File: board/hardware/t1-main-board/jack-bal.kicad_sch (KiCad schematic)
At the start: 6 parts, among them J3901 GT-3321667P-01

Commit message: Board: capture blk.mic-ambient and links #34, #35
IM73D122 on PDM CLK1 and SDI1 (BOM v1 line 34, pinout v1 AK2 and 1P2),
LR to ground, 22 Ω clock series, VDD from MIC_1V8 through link #35.
Link #34 on blk.mic-main makes the faceplate branch the rail MIC_1V8_FP
for contact 40 (power tree §4.12, G10). kicad-lib moves to e46bda4 for
the IM73D122, TPS3808G01, SN74LVC1G58 and BAT54 parts.

Co-Authored-By: Claude Opus 5.5 <noreply@anthropic.com>
Claude-Session: https://claude.ai/code/session_01Ei262h3TpgY9vyfNLMi5Mn
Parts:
- removed D3901, D3902, D3903, D3904, D3905: TPD1E10B06, Package_SON:Texas_DPY0002A_0.6x1mm_P0.65mm, symbol Device:D_TVS
- removed J3901: GT-3321667P-01, G_Switch:G_Switch_GT-3321667P-01_Jack_4.4mm_5Pole_Horizontal, symbol G_Switch:GT-3321667P-01
- added D4001, D4002, D4003, D4004, D4005: TPD1E10B06, Package_SON:Texas_DPY0002A_0.6x1mm_P0.65mm, symbol Device:D_TVS
- added J4001: GT-3321667P-01, G_Switch:G_Switch_GT-3321667P-01_Jack_4.4mm_5Pole_Horizontal, symbol G_Switch:GT-3321667P-01
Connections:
- net GND: now also D4001.1 (A1), D4002.1 (A1), D4003.1 (A1), D4004.1 (A1), D4005.1 (A1), J4001.1 (GND), J4001.9 (SWITCH)
- net HPBAL_L_N: now also D4002.2 (A2), J4001.6 (L-)
- net HPBAL_L_P: now also D4001.2 (A2), J4001.7 (L+), J4001.8 (L+)
- net HPBAL_R_N: now also D4004.2 (A2), J4001.2 (R-), J4001.3 (R-)
- net HPBAL_R_P: now also D4003.2 (A2), J4001.4 (R+), J4001.5 (R+)
- net HP_DET_BAL: now also D4005.2 (A2), J4001.10 (DETECT)
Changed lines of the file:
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@@
 (title_block (title "4.4 mm headphone jack") (date "2026-10-25") (rev "A") (company "The OpenDAP Project") (comment 1 "blk.jack-bal") (comment 2 "Balanced output jack (JEITA RC-8141C) with ESD and plug detect"))
 (symbol (lib_id "G_Switch:GT-3321667P-01") (at 52.07 64.77 0) (unit 1) (body_style 1) (exclude_from_sim no) (in_bom yes) (on_board yes) (dnp no)
-  (property "Reference" "J3901" (at 43.18 43.18 0) (effects (font (size 1.27 1.27)) (justify left)))
+  (property "Reference" "J4001" (at 43.18 43.18 0) (effects (font (size 1.27 1.27)) (justify left)))
   (property "Value" "GT-3321667P-01" (at 43.18 40.64 0) (effects (font (size 1.27 1.27)) (justify left)))
   (property "Footprint" "G_Switch:G_Switch_GT-3321667P-01_Jack_4.4mm_5Pole_Horizontal" (at 52.07 64.77 0) (effects (font (size 1.27 1.27))) (hide yes))
@@
   (pin "9")
   (pin "1")
-  (instances (project "t1-main-board" (path "/7746052e-d7f9-59ad-ba73-bd2b74439529/a72b1e0d-1505-538d-aeb6-7a353f1fd100" (reference "J3901") (unit 1))))
+  (instances (project "t1-main-board" (path "/7746052e-d7f9-59ad-ba73-bd2b74439529/a72b1e0d-1505-538d-aeb6-7a353f1fd100" (reference "J4001") (unit 1))))
 )
 (wire (pts (xy 39.37 52.07) (xy 36.83 52.07)) (stroke (width 0) (type default)))
@@
 (text "4.4 mm jack (GT-3321667P-01)" (exclude_from_sim no) (at 24.13 34.29 0) (effects (font (size 2.54 2.54)) (justify left bottom)))
 (symbol (lib_id "Device:D_TVS") (at 102.87 57.15 90) (unit 1) (body_style 1) (exclude_from_sim no) (in_bom yes) (on_board yes) (dnp no)
-  (property "Reference" "D3901" (at 108.31 55.88 90) (effects (font (size 1.27 1.27))))
+  (property "Reference" "D4001" (at 108.31 55.88 90) (effects (font (size 1.27 1.27))))
   (property "Value" "TPD1E10B06" (at 111.21 58.42 90) (effects (font (size 1.27 1.27))))
   (property "Footprint" "Package_SON:Texas_DPY0002A_0.6x1mm_P0.65mm" (at 102.87 57.15 0) (effects (font (size 1.27 1.27))) (hide yes))
@@
   (pin "1")
   (pin "2")
-  (instances (project "t1-main-board" (path "/7746052e-d7f9-59ad-ba73-bd2b74439529/a72b1e0d-1505-538d-aeb6-7a353f1fd100" (reference "D3901") (unit 1))))
+  (instances (project "t1-main-board" (path "/7746052e-d7f9-59ad-ba73-bd2b74439529/a72b1e0d-1505-538d-aeb6-7a353f1fd100" (reference "D4001") (unit 1))))
 )
 (wire (pts (xy 102.87 53.34) (xy 102.87 50.8)) (stroke (width 0) (type default)))
@@
 )
 (symbol (lib_id "Device:D_TVS") (at 125.73 57.15 90) (unit 1) (body_style 1) (exclude_from_sim no) (in_bom yes) (on_board yes) (dnp no)
-  (property "Reference" "D3902" (at 131.17 55.88 90) (effects (font (size 1.27 1.27))))
+  (property "Reference" "D4002" (at 131.17 55.88 90) (effects (font (size 1.27 1.27))))
   (property "Value" "TPD1E10B06" (at 134.07 58.42 90) (effects (font (size 1.27 1.27))))
   (property "Footprint" "Package_SON:Texas_DPY0002A_0.6x1mm_P0.65mm" (at 125.73 57.15 0) (effects (font (size 1.27 1.27))) (hide yes))
@@
   (pin "1")
   (pin "2")
-  (instances (project "t1-main-board" (path "/7746052e-d7f9-59ad-ba73-bd2b74439529/a72b1e0d-1505-538d-aeb6-7a353f1fd100" (reference "D3902") (unit 1))))
+  (instances (project "t1-main-board" (path "/7746052e-d7f9-59ad-ba73-bd2b74439529/a72b1e0d-1505-538d-aeb6-7a353f1fd100" (reference "D4002") (unit 1))))
 )
 (wire (pts (xy 125.73 53.34) (xy 125.73 50.8)) (stroke (width 0) (type default)))
@@
 )
 (symbol (lib_id "Device:D_TVS") (at 148.59 57.15 90) (unit 1) (body_style 1) (exclude_from_sim no) (in_bom yes) (on_board yes) (dnp no)
-  (property "Reference" "D3903" (at 154.03 55.88 90) (effects (font (size 1.27 1.27))))
+  (property "Reference" "D4003" (at 154.03 55.88 90) (effects (font (size 1.27 1.27))))
   (property "Value" "TPD1E10B06" (at 156.93 58.42 90) (effects (font (size 1.27 1.27))))
   (property "Footprint" "Package_SON:Texas_DPY0002A_0.6x1mm_P0.65mm" (at 148.59 57.15 0) (effects (font (size 1.27 1.27))) (hide yes))
@@
   (pin "1")
   (pin "2")
-  (instances (project "t1-main-board" (path "/7746052e-d7f9-59ad-ba73-bd2b74439529/a72b1e0d-1505-538d-aeb6-7a353f1fd100" (reference "D3903") (unit 1))))
+  (instances (project "t1-main-board" (path "/7746052e-d7f9-59ad-ba73-bd2b74439529/a72b1e0d-1505-538d-aeb6-7a353f1fd100" (reference "D4003") (unit 1))))
 )
 (wire (pts (xy 148.59 53.34) (xy 148.59 50.8)) (stroke (width 0) (type default)))
@@
 )
 (symbol (lib_id "Device:D_TVS") (at 171.45 57.15 90) (unit 1) (body_style 1) (exclude_from_sim no) (in_bom yes) (on_board yes) (dnp no)
-  (property "Reference" "D3904" (at 176.89 55.88 90) (effects (font (size 1.27 1.27))))
+  (property "Reference" "D4004" (at 176.89 55.88 90) (effects (font (size 1.27 1.27))))
   (property "Value" "TPD1E10B06" (at 179.79 58.42 90) (effects (font (size 1.27 1.27))))
   (property "Footprint" "Package_SON:Texas_DPY0002A_0.6x1mm_P0.65mm" (at 171.45 57.15 0) (effects (font (size 1.27 1.27))) (hide yes))
@@
   (pin "1")
   (pin "2")
-  (instances (project "t1-main-board" (path "/7746052e-d7f9-59ad-ba73-bd2b74439529/a72b1e0d-1505-538d-aeb6-7a353f1fd100" (reference "D3904") (unit 1))))
+  (instances (project "t1-main-board" (path "/7746052e-d7f9-59ad-ba73-bd2b74439529/a72b1e0d-1505-538d-aeb6-7a353f1fd100" (reference "D4004") (unit 1))))
 )
 (wire (pts (xy 171.45 53.34) (xy 171.45 50.8)) (stroke (width 0) (type default)))
@@
 )
 (symbol (lib_id "Device:D_TVS") (at 194.31 57.15 90) (unit 1) (body_style 1) (exclude_from_sim no) (in_bom yes) (on_board yes) (dnp no)
-  (property "Reference" "D3905" (at 199.75 55.88 90) (effects (font (size 1.27 1.27))))
+  (property "Reference" "D4005" (at 199.75 55.88 90) (effects (font (size 1.27 1.27))))
   (property "Value" "TPD1E10B06" (at 202.65 58.42 90) (effects (font (size 1.27 1.27))))
   (property "Footprint" "Package_SON:Texas_DPY0002A_0.6x1mm_P0.65mm" (at 194.31 57.15 0) (effects (font (size 1.27 1.27))) (hide yes))
@@
   (pin "1")
   (pin "2")
-  (instances (project "t1-main-board" (path "/7746052e-d7f9-59ad-ba73-bd2b74439529/a72b1e0d-1505-538d-aeb6-7a353f1fd100" (reference "D3905") (unit 1))))
+  (instances (project "t1-main-board" (path "/7746052e-d7f9-59ad-ba73-bd2b74439529/a72b1e0d-1505-538d-aeb6-7a353f1fd100" (reference "D4005") (unit 1))))
 )
 (wire (pts (xy 194.31 53.34) (xy 194.31 50.8)) (stroke (width 0) (type default)))

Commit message: Board on libs v0.2.0: lower-case kebab vendor keys (HL-13)
The libs submodule moves to v0.2.0 (5f24483). Every library nickname in
the generator, the placement tool and the floorplan study follows the
key table (Texas_Instruments -> texas-instruments, OpenDAP_Device ->
opendap-generic, Rockchip and Rockchip_PMIC -> rockchip, ...); the
library tables are written from the files. Schematic and board
regenerated.

Checks: ERC 0 errors (warnings unchanged); DRC 0 errors, 605 warnings,
the same counts by type, schematic parity 0; every placement identical;
craft Q1 met; pcb tests pass; STEP export resolves every libs 3D model
(the 27 parts without a model are KiCad stock lands that have none).

Co-Authored-By: Claude Opus 5.5 <noreply@anthropic.com>
Claude-Session: https://claude.ai/code/session_01Ei262h3TpgY9vyfNLMi5Mn
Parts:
- J4001: footprint G_Switch:G_Switch_GT-3321667P-01_Jack_4.4mm_5Pole_Horizontal -> g-switch:G_Switch_GT-3321667P-01_Jack_4.4mm_5Pole_Horizontal; symbol G_Switch:GT-3321667P-01 -> g-switch:GT-3321667P-01
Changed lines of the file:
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@@
 (paper "A4")
 (title_block (title "4.4 mm headphone jack") (date "2026-10-25") (rev "A") (company "The OpenDAP Project") (comment 1 "blk.jack-bal") (comment 2 "Balanced output jack (JEITA RC-8141C) with ESD and plug detect"))
-(symbol (lib_id "G_Switch:GT-3321667P-01") (at 52.07 64.77 0) (unit 1) (body_style 1) (exclude_from_sim no) (in_bom yes) (on_board yes) (dnp no)
+(symbol (lib_id "g-switch:GT-3321667P-01") (at 52.07 64.77 0) (unit 1) (body_style 1) (exclude_from_sim no) (in_bom yes) (on_board yes) (dnp no)
   (property "Reference" "J4001" (at 43.18 43.18 0) (effects (font (size 1.27 1.27)) (justify left)))
   (property "Value" "GT-3321667P-01" (at 43.18 40.64 0) (effects (font (size 1.27 1.27)) (justify left)))
-  (property "Footprint" "G_Switch:G_Switch_GT-3321667P-01_Jack_4.4mm_5Pole_Horizontal" (at 52.07 64.77 0) (effects (font (size 1.27 1.27))) (hide yes))
+  (property "Footprint" "g-switch:G_Switch_GT-3321667P-01_Jack_4.4mm_5Pole_Horizontal" (at 52.07 64.77 0) (effects (font (size 1.27 1.27))) (hide yes))
   (property "Datasheet" "https://datasheet.lcsc.com/datasheet/pdf/b77c36e71c4d9ede06dc371db399f62a.pdf" (at 52.07 64.77 0) (effects (font (size 1.27 1.27))) (hide yes))
   (property "Description" "4.4 mm 5-pole phone jack (balanced headphone), right angle, plated-slot terminals, detect switch, 2 locating pegs" (at 52.07 64.77 0) (effects (font (size 1.27 1.27))) (hide yes))

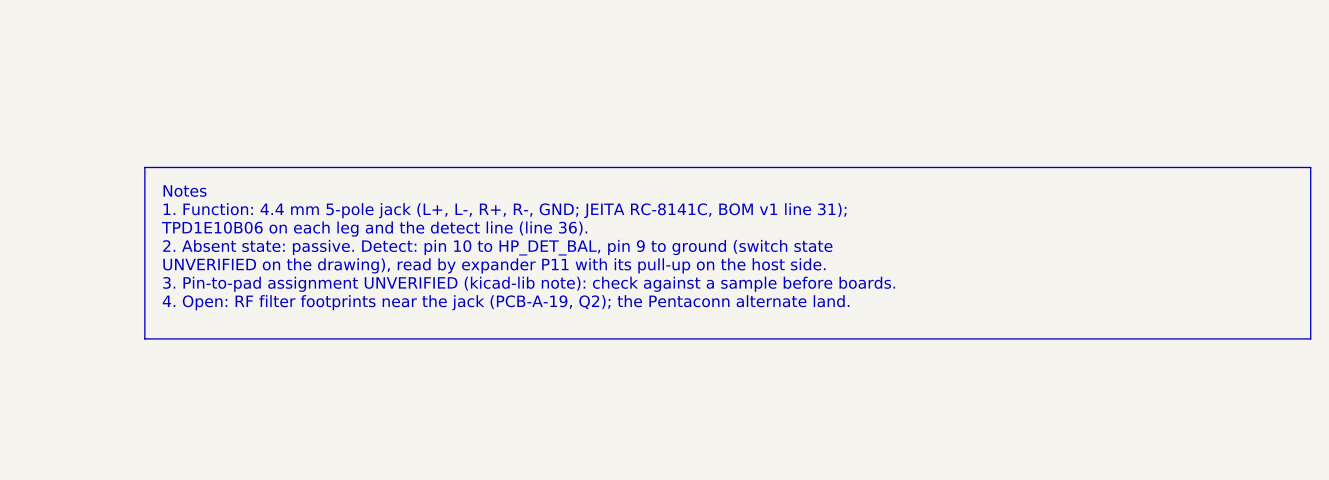
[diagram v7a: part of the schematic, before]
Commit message: Board: obsolete-audit safe fixes (BOM v1.21, power tree v0.11)
BOM quantities and owners follow the schematic (lines 34, 35, 44, 110,
121, 137); HAT input kept at 2.95 A with the DF40C-50 and the reason
recorded; power-tree HAT rows on interface v2, the PN7160 budget term
gone; SW_NODE and PCB-P-07 part lists; pinout notes; requirement,
catalog and README text; J6201; craft symmetry tables on the current
references; dead Wurth placeholder rows; stackup study inputs marked
superseded; old repository names in text and comments.

Co-Authored-By: Claude Opus 5.5 <noreply@anthropic.com>
Claude-Session: https://claude.ai/code/session_013P6pW9LdyEMFishwCcZGUr
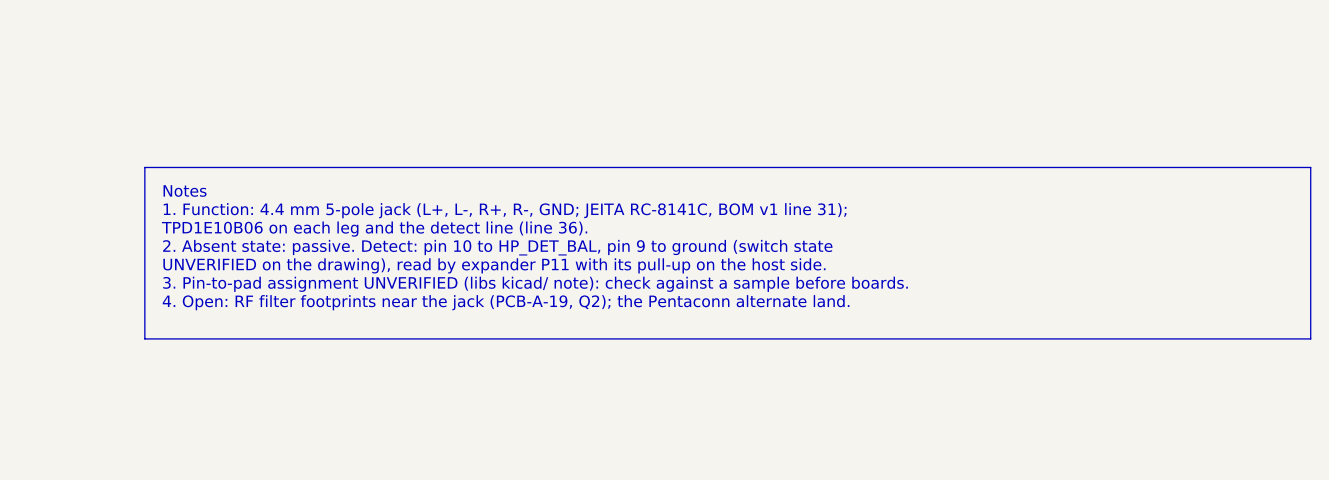
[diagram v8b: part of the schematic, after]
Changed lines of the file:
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@@
 (rectangle (start 95.25 35.56) (end 217.17 72.39) (stroke (width 0) (type dash)) (fill (type none)))
 (text "ESD (BOM v1 line 36)" (exclude_from_sim no) (at 96.52 34.29 0) (effects (font (size 2.54 2.54)) (justify left bottom)))
-(text_box "Notes\n1. Function: 4.4 mm 5-pole jack (L+, L-, R+, R-, GND; JEITA RC-8141C, BOM v1 line 31);\n   TPD1E10B06 on each leg and the detect line (line 36).\n2. Absent state: passive. Detect: pin 10 to HP_DET_BAL, pin 9 to ground (switch state\n   UNVERIFIED on the drawing), read by expander P11 with its pull-up on the host side.\n3. Pin-to-pad assignment UNVERIFIED (kicad-lib note): check against a sample before boards.\n4. Open: RF filter footprints near the jack (PCB-A-19, Q2); the Pentaconn alternate land." (exclude_from_sim no) (at 152.4 142.24 0) (size 129.54 19.05) (margins 1.905 1.905 1.905 1.905) (stroke (width 0) (type default)) (fill (type none)) (effects (font (size 1.27 1.27)) (justify left top)))
+(text_box "Notes\n1. Function: 4.4 mm 5-pole jack (L+, L-, R+, R-, GND; JEITA RC-8141C, BOM v1 line 31);\n   TPD1E10B06 on each leg and the detect line (line 36).\n2. Absent state: passive. Detect: pin 10 to HP_DET_BAL, pin 9 to ground (switch state\n   UNVERIFIED on the drawing), read by expander P11 with its pull-up on the host side.\n3. Pin-to-pad assignment UNVERIFIED (libs kicad/ note): check against a sample before boards.\n4. Open: RF filter footprints near the jack (PCB-A-19, Q2); the Pentaconn alternate land." (exclude_from_sim no) (at 152.4 142.24 0) (size 129.54 19.05) (margins 1.905 1.905 1.905 1.905) (stroke (width 0) (type default)) (fill (type none)) (effects (font (size 1.27 1.27)) (justify left top)))
 (text "Interface" (exclude_from_sim no) (at 22.86 173.99 0) (effects (font (size 2.54 2.54)) (justify left bottom)))
 (table (column_count 3) (border (external yes) (header yes) (stroke (width 0) (type solid))) (separators (rows yes) (cols yes) (stroke (width 0) (type solid))) (column_widths 45.72 25.4 50.8) (row_heights 5.08 5.08 7.62) (cells (table_cell "Net" (exclude_from_sim no) (at 22.86 175.26 0) (size 45.72 5.08) (margins 0.9525 0.9525 0.9525 0.9525) (span 1 1) (fill (type none)) (effects (font (size 1.27 1.27) (bold yes)) (justify left top))) (table_cell "Direction" (exclude_from_sim no) (at 68.58 175.26 0) (size 25.4 5.08) (margins 0.9525 0.9525 0.9525 0.9525) (span 1 1) (fill (type none)) (effects (font (size 1.27 1.27) (bold yes)) (justify left top))) (table_cell "Absent state (block not fitted)" (exclude_from_sim no) (at 93.98 175.26 0) (size 50.8 5.08) (margins 0.9525 0.9525 0.9525 0.9525) (span 1 1) (fill (type none)) (effects (font (size 1.27 1.27) (bold yes)) (justify left top))) (table_cell "HPBAL_L_P, _L_N, _R_P, _R_N" (exclude_from_sim no) (at 22.86 180.34 0) (size 45.72 5.08) (margins 0.9525 0.9525 0.9525 0.9525) (span 1 1) (fill (type none)) (effects (font (size 1.27 1.27)) (justify left top))) (table_cell "Input" (exclude_from_sim no) (at 68.58 180.34 0) (size 25.4 5.08) (margins 0.9525 0.9525 0.9525 0.9525) (span 1 1) (fill (type none)) (effects (font (size 1.27 1.27)) (justify left top))) (table_cell "Not applicable: never omitted (BRD-024)" (exclude_from_sim no) (at 93.98 180.34 0) (size 50.8 5.08) (margins 0.9525 0.9525 0.9525 0.9525) (span 1 1) (fill (type none)) (effects (font (size 1.27 1.27)) (justify left top))) (table_cell "HP_DET_BAL" (exclude_from_sim no) (at 22.86 185.42 0) (size 45.72 7.62) (margins 0.9525 0.9525 0.9525 0.9525) (span 1 1) (fill (type none)) (effects (font (size 1.27 1.27)) (justify left top))) (table_cell "Output" (exclude_from_sim no) (at 68.58 185.42 0) (size 25.4 7.62) (margins 0.9525 0.9525 0.9525 0.9525) (span 1 1) (fill (type none)) (effects (font (size 1.27 1.27)) (justify left top))) (table_cell "Pull-up on the host side; reads the detect switch" (exclude_from_sim no) (at 93.98 185.42 0) (size 50.8 7.62) (margins 0.9525 0.9525 0.9525 0.9525) (span 1 1) (fill (type none)) (effects (font (size 1.27 1.27)) (justify left top)))))
